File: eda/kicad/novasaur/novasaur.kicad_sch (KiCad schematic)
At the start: 30 parts, among them SW2 RESET, U1 74F86, U10 74F574, U11 74F574, U12 PAL16R4, U2 74F32, U3 74F11, U4 74F139, U5 74F139, U6 74F157, U7 74F175, U8 74F574, U9 74F138, X1 33M

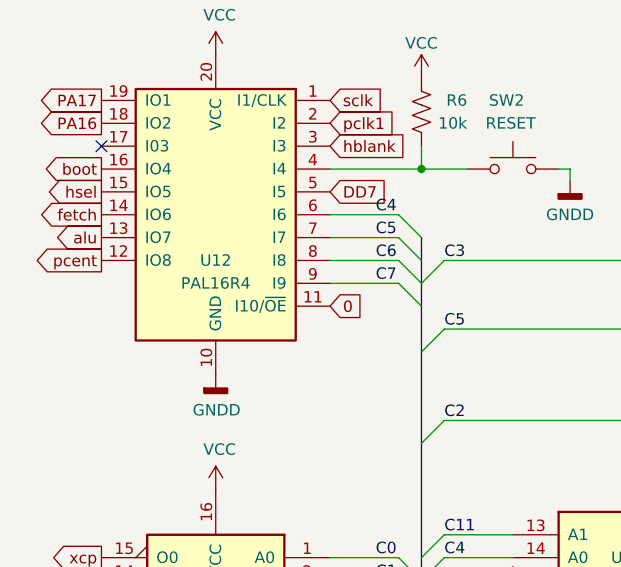
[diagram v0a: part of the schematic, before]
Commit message: Schematic updates
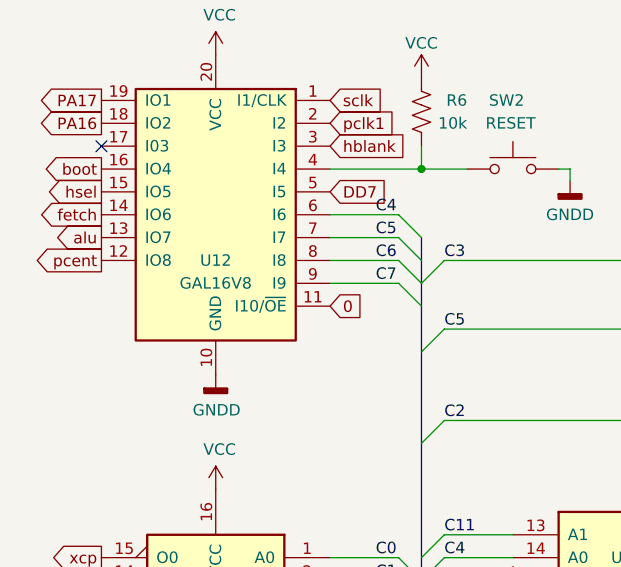
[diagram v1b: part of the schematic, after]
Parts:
- TP10: value ~EXEC -> ~{EXEC}
- TP5: value ~READ -> ~{READ}
- TP6: value ~WRITE -> ~{WRITE}
- TP7: value ~DWE -> ~{DWE}
- TP8: value ~DOE -> ~{DOE}
- TP9: value ~ALUE -> ~{ALUE}
- U12: value PAL16R4 -> GAL16V8
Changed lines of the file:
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@@
   (title_block
     (title "Novasaur Retrocomputer")
-    (date "2022-03-14")
+    (date "2022-08-07")
     (rev "1.10")
     (comment 1 "(c) Solid State Machines 2022")
@@
   (global_label "~{write}" (shape input) (at 109.22 73.66 180) (fields_autoplaced)
     (effects (font (size 1.27 1.27)) (justify right))
-    (property "Intersheet References" "${INTERSHEET_REFS}" (id 0) (at 0 0 0)
-      (effects (font (size 1.27 1.27)) hide)
+    (property "Intersheet References" "${INTERSHEET_REFS}" (id 0) (at 102.3601 73.5806 0)
+      (effects (font (size 1.27 1.27)) (justify right) hide)
     )
   )
@@
     (in_bom yes) (on_board yes)
     (property "Reference" "U12" (id 0) (at 46.99 48.26 0))
-    (property "Value" "PAL16R4" (id 1) (at 46.99 50.8 0))
+    (property "Value" "GAL16V8" (id 1) (at 46.99 50.8 0))
     (property "Footprint" "Package_DIP:DIP-20_W7.62mm_Socket_LongPads" (id 2) (at 46.99 43.18 0)
       (effects (font (size 1.27 1.27)) hide)
@@
       (effects (font (size 1.27 1.27)) (justify left))
     )
-    (property "Value" "~READ" (id 1) (at 73.66 82.55 0)
+    (property "Value" "~{READ}" (id 1) (at 73.66 82.55 0)
       (effects (font (size 1.27 1.27)) (justify left) hide)
     )
@@
       (effects (font (size 1.27 1.27)) (justify left))
     )
-    (property "Value" "~WRITE" (id 1) (at 102.87 69.85 0)
+    (property "Value" "~{WRITE}" (id 1) (at 102.87 69.85 0)
       (effects (font (size 1.27 1.27)) (justify left) hide)
     )
@@
       (effects (font (size 1.27 1.27)) (justify left))
     )
-    (property "Value" "~DWE" (id 1) (at 121.92 64.77 0)
+    (property "Value" "~{DWE}" (id 1) (at 121.92 64.77 0)
       (effects (font (size 1.27 1.27)) (justify left) hide)
     )
@@
       (effects (font (size 1.27 1.27)) (justify left))
     )
-    (property "Value" "~DOE" (id 1) (at 161.29 90.17 0)
+    (property "Value" "~{DOE}" (id 1) (at 161.29 90.17 0)
       (effects (font (size 1.27 1.27)) (justify left) hide)
     )
@@
       (effects (font (size 1.27 1.27)) (justify left))
     )
-    (property "Value" "~ALUE" (id 1) (at 106.68 57.15 0)
+    (property "Value" "~{ALUE}" (id 1) (at 106.68 57.15 0)
       (effects (font (size 1.27 1.27)) (justify left) hide)
     )
@@
       (effects (font (size 1.27 1.27)) (justify left))
     )
-    (property "Value" "~EXEC" (id 1) (at 173.99 133.35 0)
+    (property "Value" "~{EXEC}" (id 1) (at 173.99 133.35 0)
       (effects (font (size 1.27 1.27)) (justify left) hide)
     )
@@
     )
     (path "/00000000-0000-0000-0000-00005da1e9ba/00000000-0000-0000-0000-00005ee6cb33"
-      (reference "R1") (unit 1) (value "187") (footprint "Resistor_THT:R_Axial_DIN0204_L3.6mm_D1.6mm_P7.62mm_Horizontal")
+      (reference "R1") (unit 1) (value "180") (footprint "Resistor_THT:R_Axial_DIN0204_L3.6mm_D1.6mm_P7.62mm_Horizontal")
     )
     (path "/00000000-0000-0000-0000-00005da1e9c0/00000000-0000-0000-0000-00005f86c900"
@@
     )
     (path "/00000000-0000-0000-0000-00005da1e9c0/00000000-0000-0000-0000-000060e238e2"
-      (reference "R10") (unit 1) (value "374") (footprint "Resistor_THT:R_Axial_DIN0204_L3.6mm_D1.6mm_P7.62mm_Horizontal")
+      (reference "R10") (unit 1) (value "390") (footprint "Resistor_THT:R_Axial_DIN0204_L3.6mm_D1.6mm_P7.62mm_Horizontal")
     )
     (path "/00000000-0000-0000-0000-00005da1e9c0/00000000-0000-0000-0000-000060dd9233"
-      (reference "R11") (unit 1) (value "187") (footprint "Resistor_THT:R_Axial_DIN0204_L3.6mm_D1.6mm_P7.62mm_Horizontal")
+      (reference "R11") (unit 1) (value "180") (footprint "Resistor_THT:R_Axial_DIN0204_L3.6mm_D1.6mm_P7.62mm_Horizontal")
     )
     (path "/00000000-0000-0000-0000-00005da1e9c0/00000000-0000-0000-0000-00005ef89e36"
@@
     )
     (path "/00000000-0000-0000-0000-00005da1e9c0/00000000-0000-0000-0000-000060e0ab89"
-      (reference "R13") (unit 1) (value "374") (footprint "Resistor_THT:R_Axial_DIN0204_L3.6mm_D1.6mm_P7.62mm_Horizontal")
+      (reference "R13") (unit 1) (value "390") (footprint "Resistor_THT:R_Axial_DIN0204_L3.6mm_D1.6mm_P7.62mm_Horizontal")
     )
     (path "/00000000-0000-0000-0000-00005da1e9c0/00000000-0000-0000-0000-000060dc030a"
-      (reference "R14") (unit 1) (value "187") (footprint "Resistor_THT:R_Axial_DIN0204_L3.6mm_D1.6mm_P7.62mm_Horizontal")
+      (reference "R14") (unit 1) (value "180") (footprint "Resistor_THT:R_Axial_DIN0204_L3.6mm_D1.6mm_P7.62mm_Horizontal")
     )
     (path "/00000000-0000-0000-0000-00005da1e9c0/00000000-0000-0000-0000-000060df1fe3"
-      (reference "R15") (unit 1) (value "374") (footprint "Resistor_THT:R_Axial_DIN0204_L3.6mm_D1.6mm_P7.62mm_Horizontal")
+      (reference "R15") (unit 1) (value "390") (footprint "Resistor_THT:R_Axial_DIN0204_L3.6mm_D1.6mm_P7.62mm_Horizontal")
     )
     (path "/00000000-0000-0000-0000-00005da1e9c0/00000000-0000-0000-0000-000060cafe31"
-      (reference "R16") (unit 1) (value "187") (footprint "Resistor_THT:R_Axial_DIN0204_L3.6mm_D1.6mm_P7.62mm_Horizontal")
+      (reference "R16") (unit 1) (value "180") (footprint "Resistor_THT:R_Axial_DIN0204_L3.6mm_D1.6mm_P7.62mm_Horizontal")
     )
     (path "/00000000-0000-0000-0000-00005da1e9c0/00000000-0000-0000-0000-00005fcc413d"
-      (reference "R17") (unit 1) (value "187") (footprint "Resistor_THT:R_Axial_DIN0204_L3.6mm_D1.6mm_P7.62mm_Horizontal")
+      (reference "R17") (unit 1) (value "180") (footprint "Resistor_THT:R_Axial_DIN0204_L3.6mm_D1.6mm_P7.62mm_Horizontal")
     )
     (path "/00000000-0000-0000-0000-00005da1e9c0/00000000-0000-0000-0000-000060849bec"
@@
     )
     (path "/00000000-0000-0000-0000-00005e4c1851"
-      (reference "TP5") (unit 1) (value "~READ") (footprint "TestPoint:TestPoint_Pad_1.0x1.0mm")
+      (reference "TP5") (unit 1) (value "~{READ}") (footprint "TestPoint:TestPoint_Pad_1.0x1.0mm")
     )
     (path "/00000000-0000-0000-0000-00005e4c9c4c"
-      (reference "TP6") (unit 1) (value "~WRITE") (footprint "TestPoint:TestPoint_Pad_1.0x1.0mm")
+      (reference "TP6") (unit 1) (value "~{WRITE}") (footprint "TestPoint:TestPoint_Pad_1.0x1.0mm")
     )
     (path "/00000000-0000-0000-0000-00005e4d1adc"
-      (reference "TP7") (unit 1) (value "~DWE") (footprint "TestPoint:TestPoint_Pad_1.0x1.0mm")
+      (reference "TP7") (unit 1) (value "~{DWE}") (footprint "TestPoint:TestPoint_Pad_1.0x1.0mm")
     )
     (path "/00000000-0000-0000-0000-00005e4e17b0"
-      (reference "TP8") (unit 1) (value "~DOE") (footprint "TestPoint:TestPoint_Pad_1.0x1.0mm")
+      (reference "TP8") (unit 1) (value "~{DOE}") (footprint "TestPoint:TestPoint_Pad_1.0x1.0mm")
     )
     (path "/00000000-0000-0000-0000-00005e4f93ac"
-      (reference "TP9") (unit 1) (value "~ALUE") (footprint "TestPoint:TestPoint_Pad_1.0x1.0mm")
+      (reference "TP9") (unit 1) (value "~{ALUE}") (footprint "TestPoint:TestPoint_Pad_1.0x1.0mm")
     )
     (path "/00000000-0000-0000-0000-000060ed566b"
-      (reference "TP10") (unit 1) (value "~EXEC") (footprint "TestPoint:TestPoint_Pad_1.0x1.0mm")
+      (reference "TP10") (unit 1) (value "~{EXEC}") (footprint "TestPoint:TestPoint_Pad_1.0x1.0mm")
     )
     (path "/00000000-0000-0000-0000-00005da1e9ba/00000000-0000-0000-0000-00005e0a1a30"
@@
     )
     (path "/00000000-0000-0000-0000-00005da1e9ba/00000000-0000-0000-0000-00005e35ab13"
-      (reference "TP12") (unit 1) (value "~XOE") (footprint "TestPoint:TestPoint_Pad_1.0x1.0mm")
+      (reference "TP12") (unit 1) (value "~{XOE}") (footprint "TestPoint:TestPoint_Pad_1.0x1.0mm")
     )
     (path "/00000000-0000-0000-0000-00005da1e9ba/00000000-0000-0000-0000-00005dffd800"
@@
     )
     (path "/00000000-0000-0000-0000-00005da1e9ba/00000000-0000-0000-0000-00005e39ef69"
-      (reference "TP15") (unit 1) (value "~BOE") (footprint "TestPoint:TestPoint_Pad_1.0x1.0mm")
+      (reference "TP15") (unit 1) (value "~{BOE}") (footprint "TestPoint:TestPoint_Pad_1.0x1.0mm")
     )
     (path "/00000000-0000-0000-0000-00005da1e9ba/00000000-0000-0000-0000-00005dfa9e4a"
@@
     )
     (path "/00000000-0000-0000-0000-00005da1e9ba/00000000-0000-0000-0000-00005e43a381"
-      (reference "TP18") (unit 1) (value "~AOE") (footprint "TestPoint:TestPoint_Pad_1.0x1.0mm")
+      (reference "TP18") (unit 1) (value "~{AOE}") (footprint "TestPoint:TestPoint_Pad_1.0x1.0mm")
     )
     (path "/00000000-0000-0000-0000-00005da1e9ba/00000000-0000-0000-0000-00005df36352"
@@
     )
     (path "/00000000-0000-0000-0000-00005da1e9ba/00000000-0000-0000-0000-00005e39ef6f"
-      (reference "TP20") (unit 1) (value "~PGOE") (footprint "TestPoint:TestPoint_Pad_1.0x1.0mm")
+      (reference "TP20") (unit 1) (value "~{PGOE}") (footprint "TestPoint:TestPoint_Pad_1.0x1.0mm")
     )
     (path "/00000000-0000-0000-0000-00005da1e9ba/00000000-0000-0000-0000-00005dfd4631"
@@
     )
     (path "/00000000-0000-0000-0000-00005da1e9bd/00000000-0000-0000-0000-00005e24d2e2"
-      (reference "TP26") (unit 1) (value "~VOE") (footprint "TestPoint:TestPoint_Pad_1.0x1.0mm")
+      (reference "TP26") (unit 1) (value "~{VOE}") (footprint "TestPoint:TestPoint_Pad_1.0x1.0mm")
     )
     (path "/00000000-0000-0000-0000-00005da1e9bd/00000000-0000-0000-0000-00005e199218"
@@
     )
     (path "/00000000-0000-0000-0000-00005da1e80a"
-      (reference "U12") (unit 1) (value "PAL16R4") (footprint "Package_DIP:DIP-20_W7.62mm_Socket_LongPads")
+      (reference "U12") (unit 1) (value "GAL16V8") (footprint "Package_DIP:DIP-20_W7.62mm_Socket_LongPads")
     )
     (path "/00000000-0000-0000-0000-00005da1e9ba/00000000-0000-0000-0000-00005dae328a"
